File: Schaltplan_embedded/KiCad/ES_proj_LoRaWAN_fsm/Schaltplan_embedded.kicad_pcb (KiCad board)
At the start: 2 copper layers, 80 parts, among them IC1 TPS22943DCKR, IC2 BGA824N6E6327XTSA1, IC3 TESEO-LIV3F, IC4 L6924D, IC5 SPV1040T, IC6 TLS850B0TBV33ATMA1, IC7 TLS850B0TBV55ATMA1, J1 Conn_02x05_Odd_Even, J2 Conn_01x02, J3 Conn_01x08_Male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

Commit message: so
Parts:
- R4: value 1k -> 10k
- R5: value 68k -> 100k
- moved R5 386.6 mm to (402.5, -65.5)
- moved R5 6.00 mm to (286.5, -88.0)
- moved IC2 5.80 mm to (291.5, -86.0)
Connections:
- R4 pad 1: Net-(IC2-Pad16) -> GND
- R4 pad 2: VREF -> AntOFF
- R5 pad 1: GND -> +3V3
- R5 pad 2: Net-(IC2-Pad16) -> Net-(IC1-Pad3)

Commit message: Schaltplan nuevo
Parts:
- added J3: 53048-0810, SamacSys_Parts:SHDR8W35P0X125_1X8_1175X550X370P, F.Cu at (36.5, 104.5)
- J2: footprint Pin_Headers:Pin_Header_Straight_1x02_Pitch1.00mm -> Pin_Headers:Pin_Header_Straight_1x02_Pitch2.54mm
- moved Y1 466.8 mm to (59.0, 98.0), turned to 270 degrees
- moved R1 444.0 mm to (66.5, 83.0), turned to 180 degrees
- moved J2 424.3 mm to (108.0, 108.5), turned to 90 degrees
- moved C1 422.7 mm to (53.5, 93.5)
- moved C2 409.1 mm to (53.0, 99.0)
- moved U1 399.4 mm to (70.0, 97.5)
- moved J7 390.9 mm to (30.5, 67.0), turned to 180 degrees
- moved J1 386.0 mm to (107.5, 96.5), turned to 270 degrees

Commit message: neuer Schaltplan
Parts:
- removed the J3 at (336.8, -124.3)
- D2: value ESDARF02-1BU2CK -> T3V3S5-7; footprint SamacSys_Parts:ESDARF021BU2CK -> SamacSys_Parts:SODFL1608X65N
- moved C4 447.4 mm to (71.0, 75.5), turned to 90 degrees
- moved R3 443.1 mm to (85.0, 88.0), turned to 180 degrees
- moved C3 434.7 mm to (68.0, 69.0)
- moved D1 414.9 mm to (93.0, 83.5), turned to 270 degrees
- moved S1 408.3 mm to (106.5, 76.0)
- moved R2 392.3 mm to (119.0, 79.5)
- moved C6 371.7 mm to (84.3, 75.1)
- moved C5 371.1 mm to (89.8, 71.2)
- moved C13 356.5 mm to (65.0, 101.5), turned to 270 degrees
- moved C7 352.3 mm to (119.5, 85.5), turned to 270 degrees
- moved C16 347.6 mm to (71.0, 100.5), turned to 90 degrees
- moved C17 327.4 mm to (76.5, 101.0), turned to 90 degrees
- moved IC3 316.3 mm to (75.3, 120.5), turned to 270 degrees
- moved U2 315.6 mm to (148.0, 86.5)
- moved J4 296.0 mm to (206.5, 62.5), turned to 0 degrees
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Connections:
- C4 pad 2: Net-(C4-Pad2) -> GND

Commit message: layout
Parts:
- removed the R4 at (44.5, 50.5)
- removed the R5 at (402.5, -65.5)
- moved FL1 272.3 mm to (167.9, 94.1), turned to 270 degrees
- moved C20 266.0 mm to (157.4, 98.8), turned to 180 degrees
- moved C14 263.5 mm to (189.3, 94.0)
- moved C18 252.4 mm to (162.4, 67.5), turned to 180 degrees
- moved C19 252.1 mm to (181.9, 86.9), turned to 180 degrees
- moved IC1 242.7 mm to (189.1, 88.2), turned to 90 degrees
- moved IC2 213.8 mm to (176.3, 94.2)
- moved R5 199.4 mm to (196.6, 90.0), turned to 270 degrees
- moved L2 193.9 mm to (174.0, 86.4), turned to 270 degrees
- moved C12 193.6 mm to (167.4, 73.9)
- moved C11 188.8 mm to (174.7, 73.8)
- moved C10 185.3 mm to (189.3, 81.8)
- moved R4 183.6 mm to (196.2, 83.2), turned to 180 degrees
- moved L1 182.6 mm to (182.8, 75.1), turned to 270 degrees
- moved D2 7.59 mm to (194.4, 75.2), turned to 270 degrees
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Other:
- net class 3V3 added: clearance 0.15, trace_width 0.15, via_dia 0.9, via_drill 0.6
- net class 5V added: clearance 0.15, trace_width 0.15, via_dia 0.9, via_drill 0.6
- net class Data added: clearance 0.1, trace_width 0.1, via_dia 0.9, via_drill 0.6
- net class Default: clearance 0.2 -> 0.1; trace_width 0.25 -> 0.1; via_dia 0.8 -> 0.9; via_drill 0.4 -> 0.6
- rule trace_clearance: 0.2 -> 0.1
- rule trace_min: 0.2 -> 0.1
- rule via_min_drill: 0.3 -> 0.6
- rule via_min_size: 0.4 -> 0.9

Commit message: pcb erweitert
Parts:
- moved J4 187.5 mm to (20.5, 86.5), turned to 180 degrees
- moved J5 186.2 mm to (20.5, 73.0), turned to 180 degrees
- moved D2 162.4 mm to (32.0, 79.0), turned to 0 degrees
- moved C10 157.3 mm to (32.0, 86.0), turned to 180 degrees
- moved C14 157.3 mm to (32.0, 89.5), turned to 180 degrees
- moved L1 150.9 mm to (32.0, 82.0), turned to 0 degrees
- moved IC1 148.6 mm to (40.5, 87.5), turned to 0 degrees
- moved R5 148.6 mm to (48.0, 89.5), turned to 0 degrees
- moved R4 148.3 mm to (48.0, 85.0)
- moved C11 142.7 mm to (32.0, 76.0), turned to 180 degrees
- moved C12 127.2 mm to (40.5, 82.0)
- moved L2 126.0 mm to (48.0, 82.0), turned to 0 degrees
- moved C19 125.9 mm to (56.0, 89.5), turned to 0 degrees
- moved FL1 124.5 mm to (44.5, 78.0), turned to 180 degrees
- moved IC2 121.0 mm to (55.8, 83.6), turned to 270 degrees
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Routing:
- net +3V3: track 0.00 -> 132.9 mm
- net Net-(J4-Pad5): track 0.00 -> 102.2 mm
- net V_BAT: track 0.00 -> 78.6 mm, vias 0 -> 2
- net V_SUPPLY: track 0.00 -> 42.1 mm
- net SPI1_SCK: track 0.00 -> 38.8 mm
- net SPI1_MOSI: track 0.00 -> 35.5 mm
- net SPI1_MISO: track 0.00 -> 33.6 mm
- net LoRa_DI03: track 0.00 -> 31.8 mm
- net LoRa_DI04: track 0.00 -> 29.5 mm
- net Net-(C11-Pad2): track 0.00 -> 28.2 mm
- net Net-(C2-Pad2): track 0.00 -> 25.6 mm
- net LoRa_DI00: track 0.00 -> 25.5 mm
- net JTAG_TDO: track 0.00 -> 24.6 mm
- net UART_5_TX: track 0.00 -> 23.9 mm
- net LoRa_DI01: track 0.00 -> 23.7 mm
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
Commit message: schaltplan
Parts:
- moved J1 7.91 mm to (60.5, 52.5), turned to 0 degrees
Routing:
- net JTAG_RESET: track 0.00 -> 46.8 mm, vias 0 -> 1
- net JTAG_TDO: track 24.6 -> 0.00 mm
- net +3V3: track 132.9 -> 156.6 mm, vias 0 -> 1
- net JTAG_TDI: track 19.1 -> 0.00 mm
- net JTAG_TCK: track 12.9 -> 0.00 mm
- net Net-(IC1-Pad3): track 0.00 -> 12.2 mm
- net Net-(C10-Pad1): track 8.00 -> 14.6 mm
- net V_BAT: track 78.6 -> 81.6 mm, vias 2 -> 3
- net Net-(J4-Pad5): track 102.2 -> 101.4 mm, vias 0 -> 1
- net Net-(C11-Pad2): track 28.2 -> 28.0 mm, vias 0 -> 1
- net USART_3_RX: vias 0 -> 1
- net USART_3_TX: vias 0 -> 1

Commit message: Ruteado semi listo
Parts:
- moved J2 2.00 mm to (66.5, 85.0)
- moved C5 1.41 mm to (48.0, 75.0)
- moved C2 1.12 mm to (36.0, 70.5)
- moved C1 1.00 mm to (44.5, 70.5)
- moved D1 0.79 mm to (78.0, 75.0)
- moved R3 0.79 mm to (73.0, 75.0)
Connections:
- IC3 pad 13: Net-(IC3-Pad13) -> (no net)
- IC3 pad 14: Net-(IC3-Pad14) -> (no net)
- IC3 pad 15: Net-(IC3-Pad15) -> (no net)
- IC3 pad 16: Net-(IC3-Pad16) -> (no net)
- IC3 pad 17: Net-(IC3-Pad17) -> (no net)
- IC3 pad 18: Net-(IC3-Pad18) -> (no net)
- IC3 pad 4: Net-(IC3-Pad4) -> (no net)
- IC4 pad 14: Net-(IC4-Pad14) -> (no net)
- IC4 pad 16: Net-(IC4-Pad16) -> (no net)
- IC4 pad 17: Net-(IC4-Pad17) -> (no net)
- IC4 pad 9: Net-(IC4-Pad9) -> (no net)
- IC6 pad 4: Net-(IC6-Pad4) -> (no net)
- IC6 pad 6: Net-(IC6-Pad6) -> (no net)
- IC7 pad 4: Net-(IC7-Pad4) -> (no net)
- IC7 pad 6: Net-(IC7-Pad6) -> (no net)
- J1 pad 4: Net-(J1-Pad4) -> (no net)
- J1 pad 8: Net-(J1-Pad8) -> (no net)
- J3 pad 1: Net-(J3-Pad1) -> (no net)
- J3 pad 3: Net-(J3-Pad3) -> (no net)
- J3 pad 4: Net-(J3-Pad4) -> (no net)
- J3 pad 5: Net-(J3-Pad5) -> (no net)
- U1 pad 10: Net-(U1-Pad10) -> (no net)
- U1 pad 11: Net-(U1-Pad11) -> (no net)
- U1 pad 16: Net-(U1-Pad16) -> AntOFF
- U1 pad 2: Net-(U1-Pad2) -> (no net)
- U1 pad 20: Net-(U1-Pad20) -> (no net)
- U1 pad 28: Net-(U1-Pad28) -> (no net)
- U1 pad 29: Net-(U1-Pad29) -> (no net)
- U1 pad 3: Net-(U1-Pad3) -> (no net)
- U1 pad 30: Net-(U1-Pad30) -> (no net)
- U1 pad 33: Net-(U1-Pad33) -> (no net)
- U1 pad 37: Net-(U1-Pad37) -> (no net)
- U1 pad 39: Net-(U1-Pad39) -> (no net)
- U1 pad 4: Net-(U1-Pad4) -> (no net)
- U1 pad 51: Net-(U1-Pad51) -> (no net)
- U1 pad 52: Net-(U1-Pad52) -> (no net)
- U1 pad 57: Net-(U1-Pad57) -> (no net)
- U1 pad 59: Net-(U1-Pad59) -> (no net)
- U1 pad 61: AntOFF -> (no net)
- U1 pad 62: Net-(U1-Pad62) -> (no net)
- U1 pad 8: Net-(U1-Pad8) -> (no net)
- U1 pad 9: Net-(U1-Pad9) -> (no net)
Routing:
- net BAT_STAT2: track 0.00 -> 80.5 mm, vias 0 -> 2
- net 5V_ENABLE: track 0.00 -> 80.4 mm, vias 0 -> 2
- net BAT_STAT1: track 0.00 -> 79.0 mm, vias 0 -> 2
- net UART_4_RX: track 0.00 -> 45.6 mm, vias 0 -> 1
- net UART_4_TX: track 0.00 -> 45.1 mm, vias 0 -> 1
- net SPI1_NSS: track 0.00 -> 44.5 mm, vias 0 -> 2
- net GPS_RSTN: track 0.00 -> 43.5 mm, vias 0 -> 2
- net GPS_WAKEUP: track 0.00 -> 43.3 mm, vias 0 -> 2
- net RF_IN: track 0.00 -> 38.6 mm
- net LoRa_DI05: track 0.00 -> 35.3 mm, vias 0 -> 2
- net JTAG_TDI: track 0.00 -> 34.9 mm, vias 0 -> 1
- net JTAG_RESET: track 46.8 -> 80.4 mm, vias 1 -> 3
- net LoRa_RESET: track 0.00 -> 33.0 mm, vias 0 -> 2
- net +3V3: track 156.6 -> 185.8 mm, vias 1 -> 2
- net JTAG_TMS: track 0.00 -> 26.0 mm, vias 0 -> 1
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
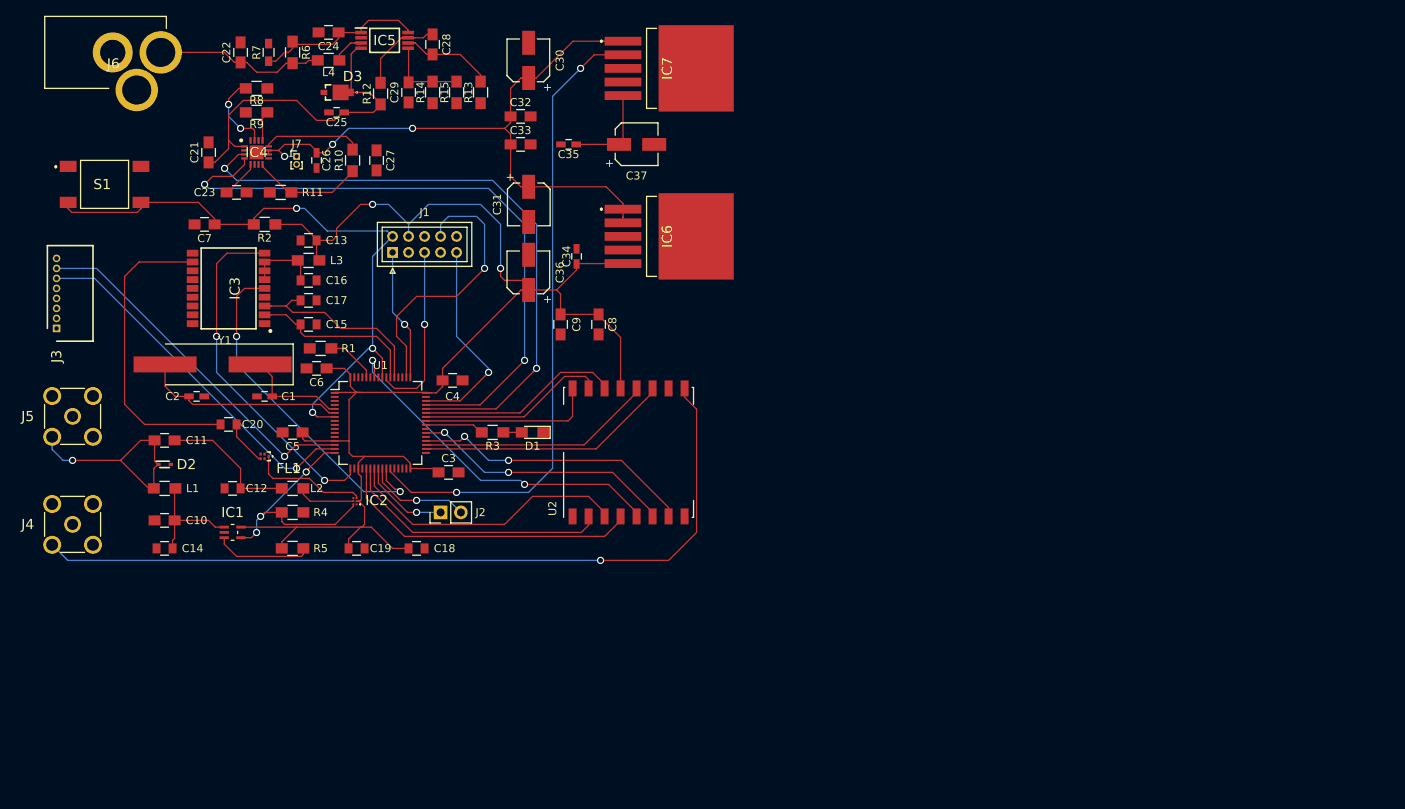
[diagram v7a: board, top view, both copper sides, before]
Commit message: Schaltplan  vervollständigt mit Massefläche
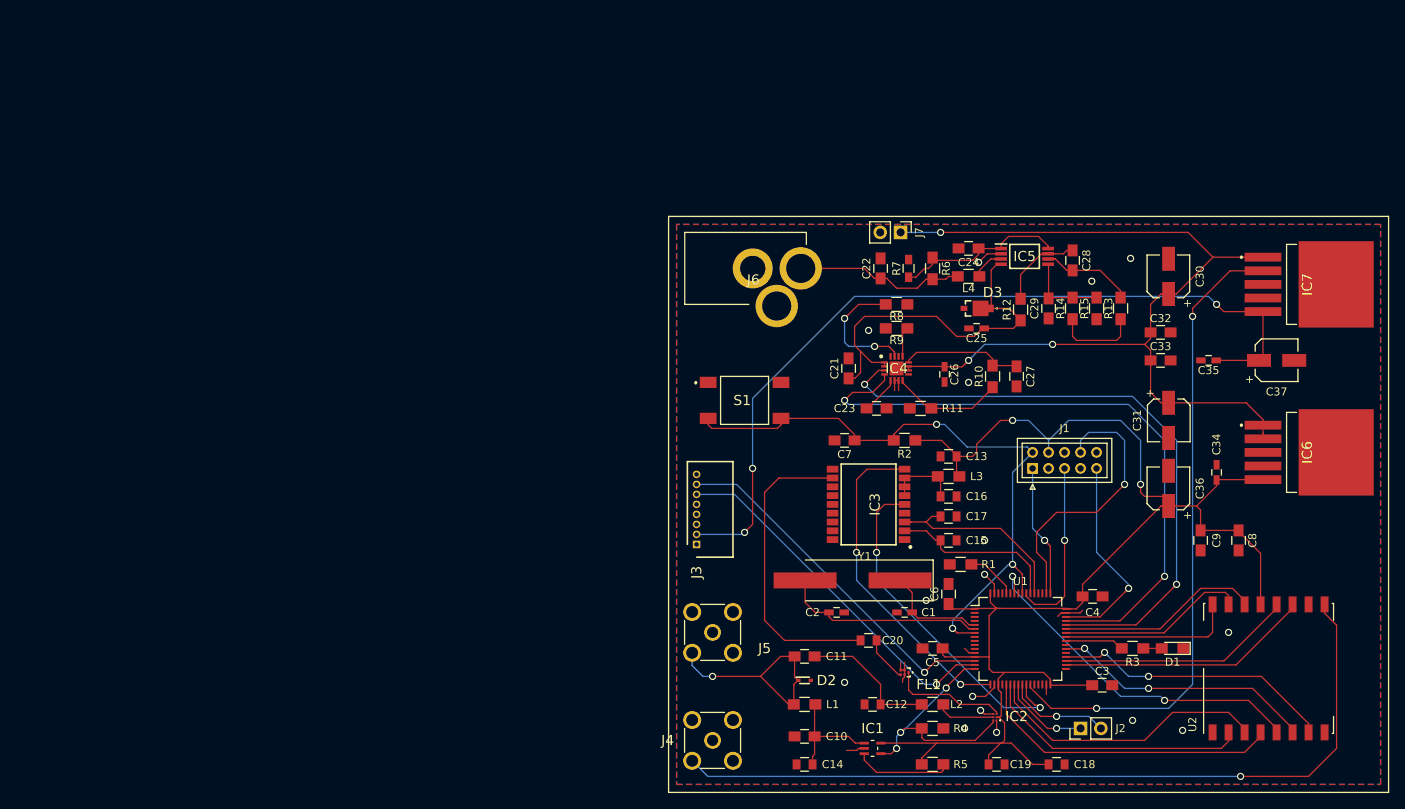
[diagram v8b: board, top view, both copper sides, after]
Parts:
- J7: value Conn_01x02_Female -> Conn_01x02; footprint Pin_Headers:Pin_Header_Straight_1x02_Pitch1.00mm -> Pin_Headers:Pin_Header_Straight_1x02_Pitch2.54mm
- moved C3 85.9 mm to (149.2, 106.6)
- moved IC2 84.4 mm to (135.8, 110.6)
- moved C1 84.4 mm to (124.5, 97.5)
- moved C10 84.4 mm to (112.0, 113.0)
- moved C11 84.4 mm to (112.0, 103.0)
- moved C12 84.4 mm to (120.5, 109.0)
- moved C13 84.4 mm to (130.0, 78.0)
- moved C14 84.4 mm to (112.0, 116.5)
- moved C15 84.4 mm to (130.0, 88.5)
- moved C16 84.4 mm to (130.0, 83.0)
- moved C17 84.4 mm to (130.0, 85.5)
- moved C18 84.4 mm to (143.5, 116.5)
- moved C19 84.4 mm to (136.0, 116.5)
- moved C2 84.4 mm to (116.0, 97.5)
- moved C20 84.4 mm to (120.0, 101.0)
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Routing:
- net +5V: track 11.7 -> 104.8 mm, vias 0 -> 3
- net V_BAT: track 81.6 -> 118.3 mm
- net GND: track 0.00 -> 28.5 mm, vias 0 -> 16
- net Net-(R13-Pad1): track 0.00 -> 10.7 mm
- net Net-(IC4-Pad15): track 10.1 -> 16.2 mm
- net V_SUPPLY: track 42.1 -> 45.8 mm
- net VREF: track 12.3 -> 15.4 mm
- net GPS_RSTN: track 43.5 -> 41.3 mm
- net +3V3: track 185.8 -> 186.9 mm
- added copper zone on B.Cu, net GND
- added copper zone on F.Cu, net GND
